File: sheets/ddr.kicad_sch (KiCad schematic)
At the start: 2 parts, among them U105 W9751G6NB-25, U301 SAM9X60-V/DWB

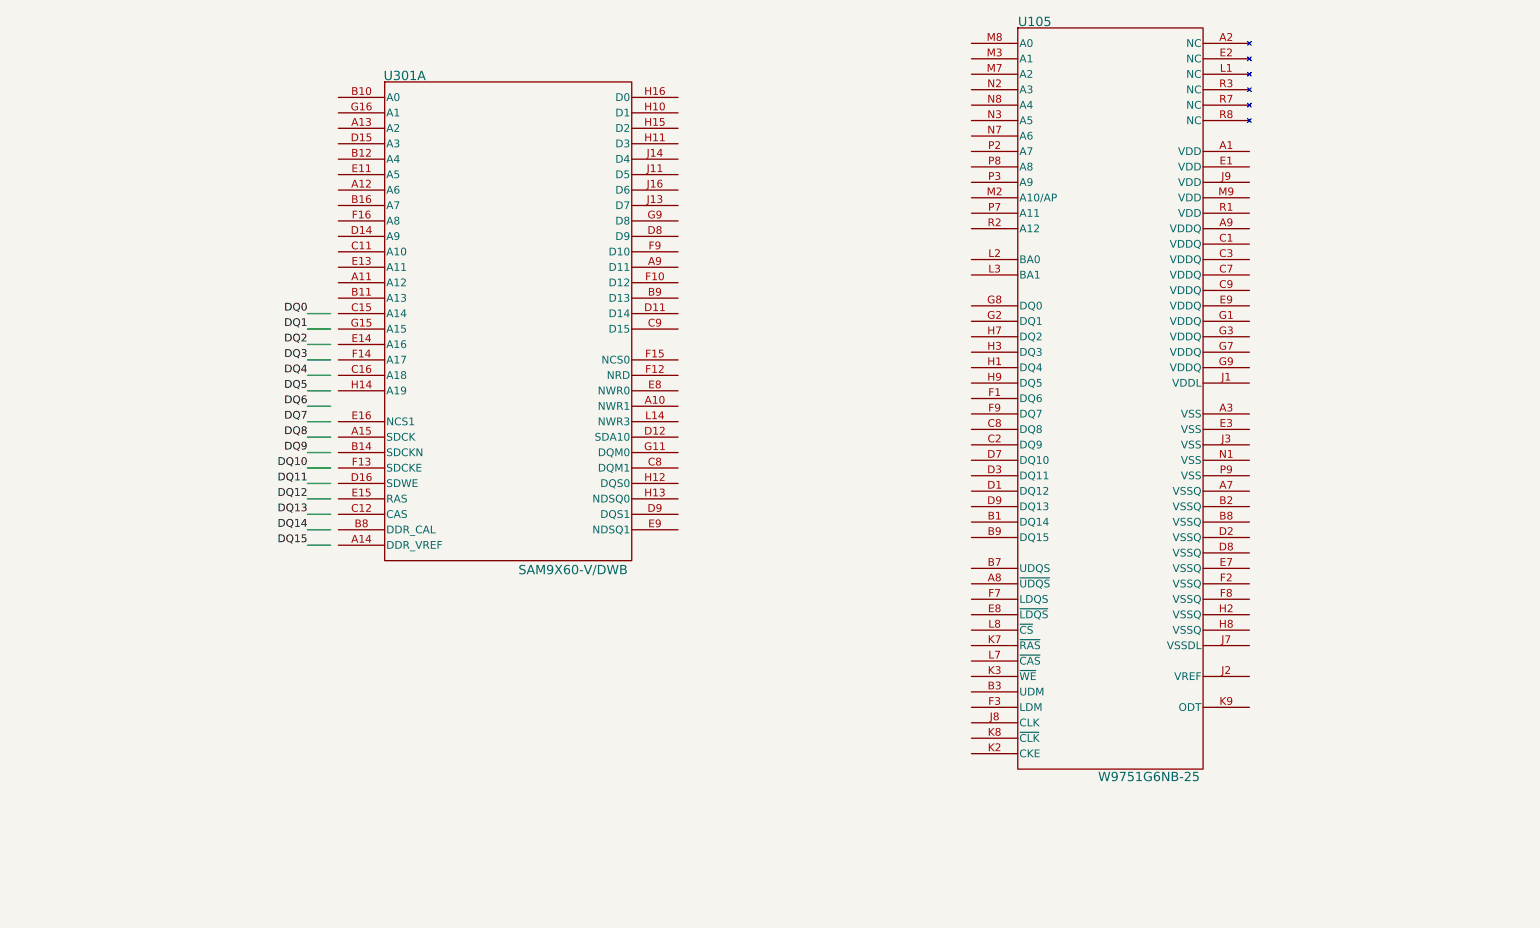
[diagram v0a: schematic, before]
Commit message: Finish DRAM schematic
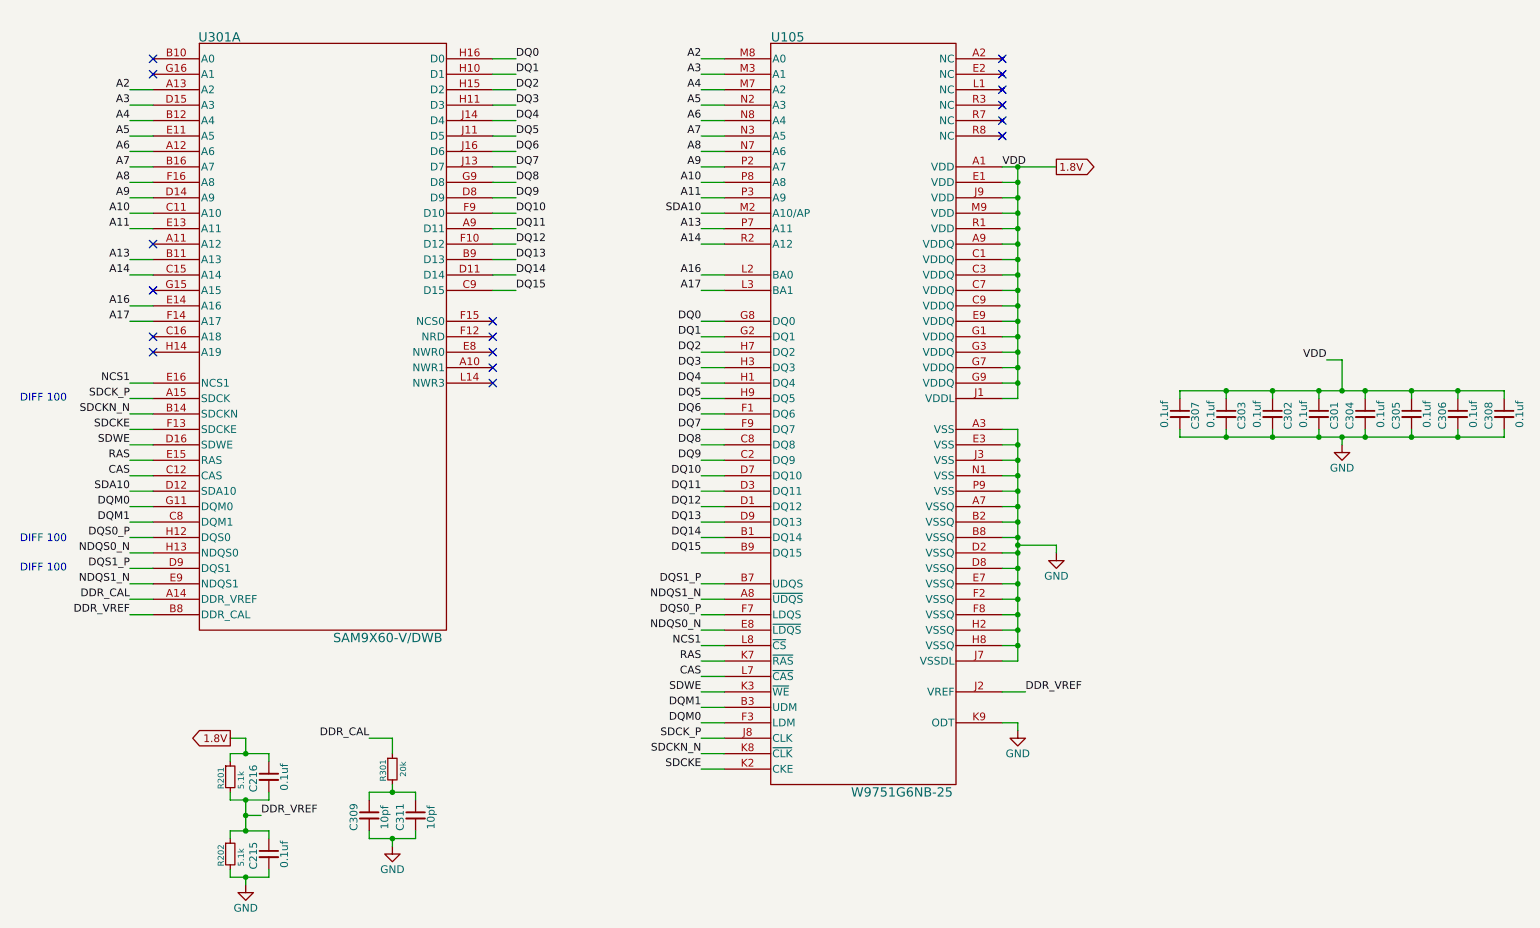
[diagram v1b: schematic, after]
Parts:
- added C215, C216, C301, C302, C303, C304, C305, C306, C307, C308: 0.1uf, Capacitor_SMD:C_0603_1608Metric_Pad1.08x0.95mm_HandSolder, symbol Device:C_Small
- added C309, C311: 10pf, Capacitor_SMD:C_0603_1608Metric_Pad1.08x0.95mm_HandSolder, symbol Device:C_Small
- added R201, R202: 5.1k, Resistor_SMD:R_0603_1608Metric_Pad0.98x0.95mm_HandSolder, symbol Device:R_Small
- added R301: 20k, Resistor_SMD:R_0603_1608Metric_Pad0.98x0.95mm_HandSolder, symbol Device:R_Small
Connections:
- net DQ0: now also U105.G8 (DQ0), U301.H16 (D0)
- net DQ1: now also U105.G2 (DQ1), U301.H10 (D1)
- net DQ10: now also U105.D7 (DQ10), U301.F9 (D10)
- net DQ11: now also U105.D3 (DQ11), U301.A9 (D11)
- net DQ12: now also U105.D1 (DQ12), U301.F10 (D12)
- net DQ13: now also U105.D9 (DQ13), U301.B9 (D13)
- net DQ14: now also U105.B1 (DQ14), U301.D11 (D14)
- net DQ15: now also U105.B9 (DQ15), U301.C9 (D15)
- net DQ2: now also U105.H7 (DQ2), U301.H15 (D2)
- net DQ3: now also U105.H3 (DQ3), U301.H11 (D3)
- net DQ4: now also U105.H1 (DQ4), U301.J14 (D4)
- net DQ5: now also U105.H9 (DQ5), U301.J11 (D5)
- net DQ6: now also U105.F1 (DQ6), U301.J16 (D6)
- net DQ7: now also U105.F9 (DQ7), U301.J13 (D7)
- net DQ8: now also U105.C8 (DQ8), U301.G9 (D8)
- net DQ9: now also U105.C2 (DQ9), U301.D8 (D9)
- net A6: now reaches U301.A12 (A6)
- net A6: now also U105.N8 (A4)
- net A2: now reaches U301.A13 (A2)
- net A2: now also U105.M8 (A0)
- net DDR_CAL: now reaches U301.A14 (DDR_VREF)
- net DDR_CAL: now also R301.1
- net SDCK_P: now reaches U301.A15 (SDCK)
- net SDCK_P: now also U105.J8 (CLK)
- net A13: now reaches U301.B11 (A13)
- net A13: now also U105.P7 (A11)
- net A4: now reaches U301.B12 (A4)
- net A4: now also U105.M7 (A2)
- net SDCKN_N: now reaches U301.B14 (SDCKN)
- net SDCKN_N: now also U105.K8 (~{CLK})
- net A7: now reaches U301.B16 (A7)
- net A7: now also U105.N3 (A5)
- net DDR_VREF: now reaches U301.B8 (DDR_CAL)
- net DDR_VREF: now also U105.J2 (VREF), C215.1, C216.2, R201.2, R202.1
- net A10: now reaches U301.C11 (A10)
- net A10: now also U105.P8 (A8)
- net CAS: now reaches U301.C12 (CAS)
- net CAS: now also U105.L7 (~{CAS})
- net A14: now reaches U301.C15 (A14)
- net A14: now also U105.R2 (A12)
- net DQM1: now reaches U301.C8 (DQM1)
- net DQM1: now also U105.B3 (UDM)
- net SDA10: now reaches U301.D12 (SDA10)
- net SDA10: now also U105.M2 (A10/AP)
- net A9: now reaches U301.D14 (A9)
- net A9: now also U105.P2 (A7)
- net A3: now reaches U301.D15 (A3)
- net A3: now also U105.M3 (A1)
- net SDWE: now reaches U301.D16 (SDWE)
- net SDWE: now also U105.K3 (~{WE})
- net DQS1_P: now reaches U301.D9 (DQS1)
- net DQS1_P: now also U105.B7 (UDQS)
- net A5: now reaches U301.E11 (A5)
- net A5: now also U105.N2 (A3)
- net A11: now reaches U301.E13 (A11)
- net A11: now also U105.P3 (A9)
- net A16: now reaches U301.E14 (A16)
- net A16: now also U105.L2 (BA0)
- net RAS: now reaches U301.E15 (RAS)
- net RAS: now also U105.K7 (~{RAS})
- net NCS1: now reaches U301.E16 (NCS1)
- net NCS1: now also U105.L8 (~{CS})
- net NDQS1_N: now reaches U301.E9 (NDQS1)
- net NDQS1_N: now also U105.A8 (~{UDQS})
- net SDCKE: now reaches U301.F13 (SDCKE)
- net SDCKE: now also U105.K2 (CKE)
- net A17: now reaches U301.F14 (A17)
- net A17: now also U105.L3 (BA1)
- net A8: now reaches U301.F16 (A8)
- net A8: now also U105.N7 (A6)
- net DQM0: now reaches U301.G11 (DQM0)
- net DQM0: now also U105.F3 (LDM)
- net DQS0_P: now reaches U301.H12 (DQS0)
- net DQS0_P: now also U105.F7 (LDQS)
- net NDQS0_N: now reaches U301.H13 (NDQS0)
- net NDQS0_N: now also U105.E8 (~{LDQS})
- net 1.8V: now reaches U105.A1 (VDD)
- net 1.8V: now also U105.A9 (VDDQ), U105.C1 (VDDQ), U105.C3 (VDDQ), U105.C7 (VDDQ), U105.C9 (VDDQ), U105.E1 (VDD), U105.E9 (VDDQ), U105.G1 (VDDQ), U105.G3 (VDDQ), U105.G7 (VDDQ), U105.G9 (VDDQ), U105.J1 (VDDL), U105.J9 (VDD), U105.M9 (VDD), U105.R1 (VDD), C216.1, C301.1, C302.1, C303.1, C304.1, C305.1, C306.1, C307.1, C308.1, R201.1
- net GND: now reaches U105.A3 (VSS)
- net GND: now also U105.A7 (VSSQ), U105.B2 (VSSQ), U105.B8 (VSSQ), U105.D2 (VSSQ), U105.D8 (VSSQ), U105.E3 (VSS), U105.E7 (VSSQ), U105.F2 (VSSQ), U105.F8 (VSSQ), U105.H2 (VSSQ), U105.H8 (VSSQ), U105.J3 (VSS), U105.J7 (VSSDL), U105.K9 (ODT), U105.N1 (VSS), U105.P9 (VSS), C215.2, C301.2, C302.2, C303.2, C304.2, C305.2, C306.2, C307.2, C308.2, C309.2, C311.2, R202.2
- new net: C309.1, C311.1, R301.2
- no-connect marks 0 -> 17
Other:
- note added: "DIFF 100"
- moved on the sheet: U105, U301A

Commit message: Update schematic
- Update VDDCORE to 1.13V
- Fix DDR_CAL circuit
- Update external load capacitor to 22pf
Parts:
- removed C311: 10pf, Capacitor_SMD:C_0603_1608Metric_Pad1.08x0.95mm_HandSolder, symbol Device:C_Small
- added R1, R2: 10k, Resistor_SMD:R_0603_1608Metric_Pad0.98x0.95mm_HandSolder, symbol Device:R_Small
- C309: value 10pf -> 22pf
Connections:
- net 1.8V: now also R1.2
- net DDR_CAL: now also C309.1
- net GND: now also R301.2, R2.1; no longer U105.K9 (ODT)
- new net: R1.1, R2.2, U105.K9 (ODT)
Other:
- moved on the sheet: C309
